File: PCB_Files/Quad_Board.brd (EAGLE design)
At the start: 129.2 x 80 mm, 32 parts, among them IC2 LM317MB, Q1 32.768kHz, Q2 KX-7 48MHz

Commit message: Board Layout Under Progress
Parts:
- removed 12V_PDB, JP1: (no value), pinhead:1X02
- removed U$2: NAZE32_FC, Naze32_FCBoard:NAZE32_BOARD_FOOTPRINT
- added LEVEL_TRANSLATOR1, LEVEL_TRANSLATOR_@, LEVEL_TRANSLATOR_@1: (no value), SparkFun-DigitalIC:SO14
- added MOTHERBOPARD_TX: (no value), pinhead:1X02
- added NAZE32_PINHEAD: (no value), pinhead:1X10
- added R4, R5, R6: (no value), eagle-ltspice:R2512
- added SJ1, SJ2, SJ3: SOLDERJUMPERNC2, SparkFun-Passives:SJ_2S-NOTRACE
- moved Q2 209.3 mm to (55.9, 44.5), turned to 90 degrees
- moved C5 209.1 mm to (54.6, 29.2), turned to 90 degrees
- moved C6 208.3 mm to (54.6, 34.3), turned to 90 degrees
- moved R3 207.8 mm to (54.6, 39.4), turned to 90 degrees
- moved MINIJTAG 206.0 mm to (64.8, 14.0), turned to 270 degrees
- moved C8 201.9 mm to (49.5, 29.2), turned to 90 degrees
- moved C11 201.1 mm to (49.5, 34.3), turned to 90 degrees
- moved C12 200.6 mm to (49.5, 39.4), turned to 90 degrees
- moved C13 200.3 mm to (49.5, 44.5), turned to 90 degrees
- moved L1 192.8 mm to (43.2, 30.5), turned to 90 degrees
- moved C3 192.2 mm to (43.2, 34.3), turned to 90 degrees
- moved C4 191.6 mm to (43.2, 39.4), turned to 90 degrees
- moved C7 191.3 mm to (43.2, 44.5), turned to 90 degrees
- moved Q1 183.0 mm to (48.3, 16.5), turned to 270 degrees
- moved R1 182.9 mm to (57.1, 6.35), turned to 90 degrees
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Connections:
- net N$17 renamed P10.5_V
- removed net 12VDC: 12V_PDB.1
- removed net N$13: ULTRA3.2
- removed net N$3: ULTRA1.2
- removed net N$4: 12V_PDB.2
- removed net N$5: ULTRA3.3
- removed net N$6: MSP1.75
- removed net P5.4_IO_J3.29: MSP1.68, ULTRA5.2
- removed net P5.5_IO_J3.30: MSP1.69, ULTRA6.2
- removed net P5.6_PWM_J4.37: MSP1.70, ULTRA5.3
- removed net P5.7_IO_J2.17: MSP1.71, ULTRA6.3
- removed net P6.6_CAPTURE_J4.36: MSP1.80
- removed net P6.7_CAPTURE_J4.35: MSP1.81
- removed net P9.1: MSP1.53, ULTRA2.2
- new net 3.3V: LEVEL_TRANSLATOR1.1, LEVEL_TRANSLATOR_@.1, LEVEL_TRANSLATOR_@1.1, SJ1.2, SJ2.2, SJ3.2
- new net 5V: LEVEL_TRANSLATOR1.14, LEVEL_TRANSLATOR_@.14, LEVEL_TRANSLATOR_@1.14
- new net N$1: MSP1.53
- new net N$19: MSP1.68
- new net N$20: MSP1.69
- new net N$25: MSP1.24
- new net N$26: MSP1.25
- new net OE: LEVEL_TRANSLATOR1.8, LEVEL_TRANSLATOR_@.8, LEVEL_TRANSLATOR_@1.8, R4.2, R5.2, R6.2, SJ1.1, SJ2.1, SJ3.1
- new net P10.3_GPIO5V: LEVEL_TRANSLATOR_@.10, ULTRA4.3
- new net P10.4_5V: LEVEL_TRANSLATOR_@.12, ULTRA3.3
- new net P10.5_5V: LEVEL_TRANSLATOR_@.11
- new net P5.6: LEVEL_TRANSLATOR_@1.2, MSP1.70
- new net P5.6_5V: LEVEL_TRANSLATOR_@1.13, ULTRA5.3
- new net P5.7: LEVEL_TRANSLATOR_@1.3
- new net P5.7/TA2.2/VREF-/VEREF-/C1.6: MSP1.71
- new net P5.7_5V: LEVEL_TRANSLATOR_@1.12, ULTRA5.2
- new net P6.6: LEVEL_TRANSLATOR_@1.4, MSP1.80
- new net P6.6_5V: LEVEL_TRANSLATOR_@1.11, ULTRA6.3
- new net P6.7: LEVEL_TRANSLATOR_@1.5, MSP1.81
- new net P6.7_5V: LEVEL_TRANSLATOR_@1.10, ULTRA6.2
- new net P8.0_5V: LEVEL_TRANSLATOR1.13, ULTRA1.2
- new net P8.1_5V: LEVEL_TRANSLATOR1.12, ULTRA1.3
- new net P8.2_5V: LEVEL_TRANSLATOR1.11
- new net P8.3_5V: ULTRA2.2
- new net P9.2_5V: LEVEL_TRANSLATOR1.10, ULTRA2.3
- new net P9.3: LEVEL_TRANSLATOR_@.2, MSP1.75
- new net P9.3_5V: LEVEL_TRANSLATOR_@.13, ULTRA3.2
- net 5VDC: now also NAZE32_PINHEAD.2; no longer U$2.5V
- net GND: now also LEVEL_TRANSLATOR1.7, LEVEL_TRANSLATOR_@.7, LEVEL_TRANSLATOR_@1.7, NAZE32_PINHEAD.1, R4.1, R5.1, R6.1; no longer U$2.GND
- net N$10: now also MOTHERBOPARD_TX.2; no longer JP1.2
- net P10.3: now also LEVEL_TRANSLATOR_@.5
- net P10.4: now also LEVEL_TRANSLATOR_@.3; no longer MSP1.24
- net P10.5: now also LEVEL_TRANSLATOR_@.4; no longer MSP1.25, ULTRA4.3
- net P2.4_PWM_J4.38: now also NAZE32_PINHEAD.10; no longer U$2.8
- net P2.5_PWM_J2.19: now also NAZE32_PINHEAD.9; no longer U$2.7
- net P2.6_PWM_J4.39: now also NAZE32_PINHEAD.8; no longer U$2.6
- net P2.7_PWM_J4.40: no longer U$2.LED/5
- net P3.3_UTXD_J1.4: now also MOTHERBOPARD_TX.1
- net P7.4: now also NAZE32_PINHEAD.6; no longer U$2.U2RX/4
- net P7.5: now also NAZE32_PINHEAD.5; no longer U$2.U2TX/3
- net P7.6: now also NAZE32_PINHEAD.4; no longer U$2.2
- net P7.7: now also NAZE32_PINHEAD.3; no longer U$2.PPM
- net P8.0: now also LEVEL_TRANSLATOR1.2
- net P8.1: now also LEVEL_TRANSLATOR1.3, LEVEL_TRANSLATOR1.4
- net P8.2: no longer ULTRA1.3
- net P9.2: now also LEVEL_TRANSLATOR1.5; no longer ULTRA2.3
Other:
- board size 129.2 x 80 mm -> 114 x 80 mm

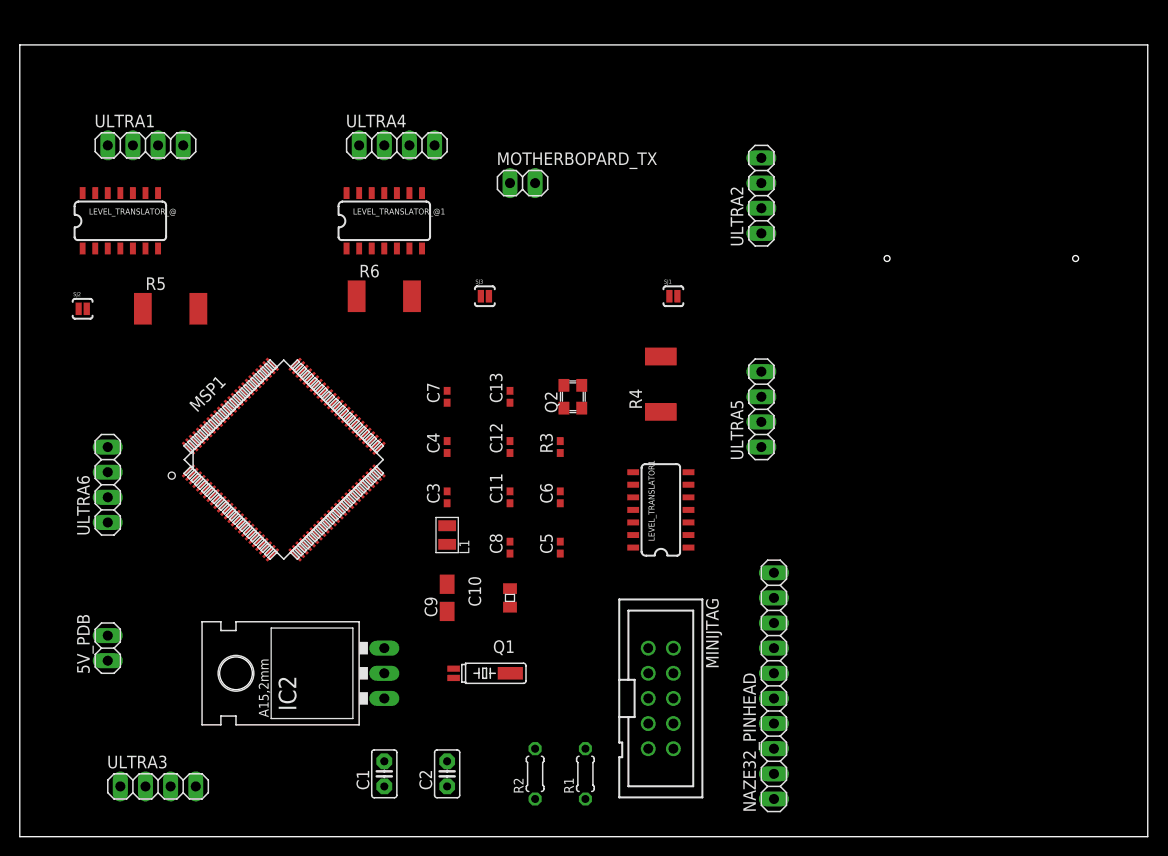
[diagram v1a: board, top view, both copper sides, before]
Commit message: Board Layout in Routing Stage
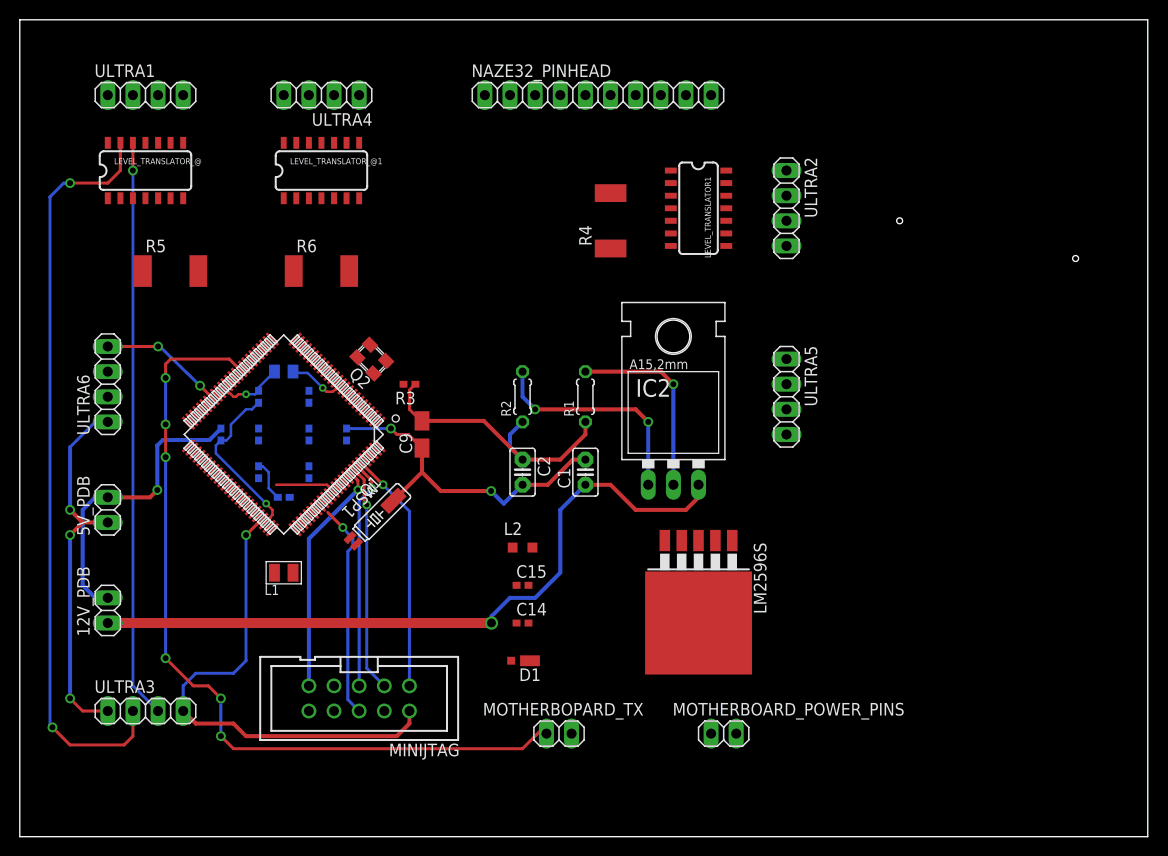
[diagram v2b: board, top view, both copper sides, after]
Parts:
- removed SJ1, SJ2, SJ3: SOLDERJUMPERNC2, SparkFun-Passives:SJ_2S-NOTRACE
- added 12V_PDB, MOTHERBOARD_POWER_PINS: (no value), pinhead:1X02
- added C14: 680u, rcl:0402
- added C15: 220u, rcl:0402
- added D1: PD3S160, diode:POWERDI323
- added L2: 33u, resistor:L2012C
- added LM2596S: LM2596S, national-semiconductor:TO263-5
- moved NAZE32_PINHEAD 62.3 mm to (58.4, 74.9), turned to 0 degrees
- moved MOTHERBOPARD_TX 55.7 mm to (54.5, 10.4)
- moved IC2 40.2 mm to (66.0, 39.4), turned to 0 degrees
- moved R2 38.1 mm to (50.8, 44.5)
- moved R1 38.1 mm to (57.1, 44.5)
- moved C1 36.6 mm to (57.1, 36.8)
- moved C10 32.3 mm to (26.7, 47.0), flipped to the bottom, turned to 0 degrees
- moved C2 31.4 mm to (50.8, 36.8), turned to 270 degrees
- moved C8 31.4 mm to (20.3, 40.6), flipped to the bottom
- moved LEVEL_TRANSLATOR1 30.7 mm to (68.6, 63.5), turned to 270 degrees
- moved MINIJTAG 30.5 mm to (34.3, 14.0), turned to 180 degrees
- moved C5 28.4 mm to (26.7, 34.3), flipped to the bottom, turned to 0 degrees
- moved C6 22.5 mm to (33.0, 40.6), flipped to the bottom
- moved Q2 20.7 mm to (35.6, 48.3), turned to 135 degrees
- moved C11 20.5 mm to (29.2, 36.8), flipped to the bottom
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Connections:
- net P3.2/PM_UCA2RXD/PM_UCA2SOMI renamed N$10
- removed net N$25: MSP1.24
- removed net N$26: MSP1.25
- removed net OE: LEVEL_TRANSLATOR1.8, LEVEL_TRANSLATOR_@.8, LEVEL_TRANSLATOR_@1.8, R4.2, R5.2, R6.2, SJ1.1, SJ2.1, SJ3.1
- removed net P5.7/TA2.2/VREF-/VEREF-/C1.6: MSP1.71
- removed net P8.3_5V: ULTRA2.2
- new net 12VDC: 12V_PDB.1, C1.1, C14.1, IC2.3, LM2596S.1
- new net MOTHEROARD_V+: C15.1, L2.2, LM2596S.4, MOTHERBOARD_POWER_PINS.1
- new net N$4: D1.C, L2.1, LM2596S.2
- net 3.3V: now also LEVEL_TRANSLATOR1.8, LEVEL_TRANSLATOR_@.8, LEVEL_TRANSLATOR_@1.8, R4.2, R5.2, R6.2; no longer SJ1.2, SJ2.2, SJ3.2
- net 5VDC: now also 5V_PDB.1; no longer C1.1, IC2.3
- net GND: now also 12V_PDB.2, C14.2, C15.2, D1.A, LM2596S.3, LM2596S.5, MOTHERBOARD_POWER_PINS.2
- net P10.4: now also MSP1.24
- net P10.5: now also MSP1.25
- net P2.7_PWM_J4.40: now also NAZE32_PINHEAD.7
- net P5.7: now also MSP1.71
- net P8.2_5V: now also ULTRA2.2
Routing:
- net GND: track 0.00 -> 144.5 mm, vias 0 -> 7
- net P3.3_UTXD_J1.4: track 0.00 -> 84.4 mm, vias 0 -> 6
- net P9.3_5V: track 0.00 -> 76.5 mm, vias 0 -> 2
- net 12VDC: track 0.00 -> 72.4 mm, vias 0 -> 1
- net P10.4_5V: track 0.00 -> 58.5 mm, vias 0 -> 1
- net 3V3: track 0.00 -> 42.2 mm, vias 0 -> 1
- net 5VDC: track 0.00 -> 38.2 mm, vias 0 -> 3
- net TCK_SWCLK: track 0.00 -> 24.5 mm, vias 0 -> 1
- net TDI: track 0.00 -> 23.8 mm, vias 0 -> 1
- net TMS_SWDIO: track 0.00 -> 23.2 mm, vias 0 -> 1
- net TDO_SWO: track 0.00 -> 23.0 mm, vias 0 -> 1
- net N$28: track 0.00 -> 22.6 mm, vias 0 -> 2
- net !RST: track 0.00 -> 21.8 mm, vias 0 -> 1
- net N$29: track 0.00 -> 19.6 mm, vias 0 -> 1
- net N$2: track 0.00 -> 6.07 mm
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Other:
- board size 114 x 80 mm -> 114 x 82.5 mm

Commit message: PCB Layout Rev1 90% done
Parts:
- added R7: (no value), rcl:0204/5
- added U$1: TXS0102, TXS0102-bi-directional-translator:SM8
- moved C15 7.41 mm to (57.1, 29.2), turned to 270 degrees
- moved C14 6.35 mm to (57.1, 21.6), turned to 90 degrees
- moved D1 3.81 mm to (50.8, 21.6), turned to 270 degrees
- moved R4 1.80 mm to (61.0, 63.5)
- moved ULTRA5 1.27 mm to (77.5, 45.7)
- turned C1 to 270 degrees
- turned L2 to 90 degrees
- turned R5 to 180 degrees
- turned R6 to 180 degrees
- renumbered LEVEL_TRANSLATOR_@ to LEVEL_TRANSLATOR_2, LEVEL_TRANSLATOR_@1 to LEVEL_TRANSLATOR_3
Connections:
- removed net N$10: MSP1.34
- removed net N$3: MOTHERBOPARD_TX.2
- removed net P3.3_UTXD_J1.4: MOTHERBOPARD_TX.1, MSP1.35
- new net A1: MSP1.35, U$1.5
- new net A2: MOTHERBOPARD_TX.1, U$1.4
- new net B1: MSP1.34, U$1.8
- new net B2: MOTHERBOPARD_TX.2, U$1.1
- new net OE: R7.1, U$1.6
- net 3V3: now also U$1.7
- net 5V: now also U$1.3
- net GND: now also R7.2, U$1.2
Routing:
- net GND: track 144.5 -> 345.1 mm, vias 7 -> 22
- net 5V: track 0.00 -> 85.2 mm, vias 0 -> 6
- net P9.2: track 0.00 -> 84.7 mm, vias 0 -> 6
- net P3.3_UTXD_J1.4: track 84.4 -> 0.00 mm, vias 6 -> 0
- net 3.3V: track 0.00 -> 83.8 mm, vias 0 -> 12
- net P8.1: track 0.00 -> 77.5 mm, vias 0 -> 4
- net P8.0_5V: track 0.00 -> 70.3 mm, vias 0 -> 4
- net P2.4_PWM_J4.38: track 0.00 -> 70.3 mm, vias 0 -> 3
- net 5VDC: track 38.2 -> 106.2 mm, vias 3 -> 4
- net P9.3: track 0.00 -> 66.5 mm, vias 0 -> 4
- net P2.5_PWM_J2.19: track 0.00 -> 65.8 mm, vias 0 -> 1
- net P2.6_PWM_J4.39: track 0.00 -> 65.0 mm, vias 0 -> 5
- net P7.4: track 0.00 -> 58.9 mm, vias 0 -> 1
- net P7.5: track 0.00 -> 57.4 mm, vias 0 -> 1
- net P2.7_PWM_J4.40: track 0.00 -> 56.9 mm, vias 0 -> 1
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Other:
- board size 114 x 82.5 mm -> 83.5 x 78.7 mm
- board text added: "3-DMQ System PCB Layout"
- board text added: "rev 1.0"

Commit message: MCU Icaps routing remaining
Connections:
- net N$19 renamed P5.4/A1
- net N$20 renamed P5.5/A0
- net P1.0_LED1 renamed P1.0/UCA0STE
- net P1.1_BUTTON1 renamed P1.1/UCA0CLK
- net P1.2_BCLUART_RXD renamed P1.2/UCA0RXD/UCA0SOMI
- net P1.3_BCLUART_TXD renamed P1.3/UCA0TXD/UCA0SIMO
- net P1.4_BUTTON2 renamed P1.4/UCB0STE
- net P1.5_SPICLK_J1.7 renamed P1.5/UCB0CLK
- net P1.6_SPIMOSI_J2.15 renamed P1.6/UCB0SIMO/UCB0SDA
- net P1.7_SPIMISO_J2.14 renamed P1.7/UCB0SOMI/UCB0SCL
- net P2.0_RGBLED_RED renamed P2.0/PM_UCA1STE
- net P2.1_RGBLED_GREEN renamed P2.1/PM_UCA1CLK
- net P2.2_RGBLED_BLUE renamed P2.2/PM_UCA1RXD/PM_UCA1SOMI
- net P2.3_IO_J4.34 renamed P2.3/PM_UCA1TXD/PM_UCA1SIMO
- net P3.0_IO_J2.18 renamed P3.0/PM_UCA2STE
- net P3.1_BCLUART_RTS renamed P3.1/PM_UCA2CLK
- net P3.4_BCLUART_CTS renamed P3.4/PM_UCB2STE
- net P3.5_IO_J4.32 renamed P3.5/PM_UCB2CLK
- net P3.6_IO_J2.11 renamed P3.6/PM_UCB2SIMO/PM_UCB2SDA
- net P3.7_IO_J4.31 renamed P3.7/PM_UCB2SOMI/PM_UCB2SCL
- net P4.0_A13_J3.24 renamed P4.0/A13
- net P4.1_IO_J1.5 renamed P4.1/A12
- net P4.2_A11_J3.25 renamed P4.2/ACLK/TA2CLK/A11
- net P4.3_A10_J1.6 renamed P4.3/MCLK/RTCCLK/A10
- net P4.4_A9_J3.26 renamed P4.4/HSMCLK/SVMHOUT/A9
- net P4.5_A8_J3.27 renamed P4.5/A8
- net P4.6_IO_J1.8 renamed P4.6/A7
- net P4.7_A6_J3.28 renamed P4.7/A6
- net P5.0_IO_J2.13 renamed P5.0/A5
- net P5.1_IO_J4.33 renamed P5.1/A4
- net P5.2_IO_J2.12 renamed P5.2/A3
- net P5.3 renamed P5.3/A2
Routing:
- net P8.1_5V: track 0.00 -> 81.4 mm, vias 0 -> 3
- net 5V: track 85.2 -> 155.5 mm, vias 6 -> 10
- net 5VDC: track 106.2 -> 162.1 mm, vias 4 -> 5
- net 3.3V: track 83.8 -> 112.3 mm
- net GND: track 345.1 -> 355.7 mm

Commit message: PCB Updates
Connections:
- net N$1 renamed P9.1/A16
- net P10.0 renamed P10.0/UCB3STE
- net P10.1 renamed P10.1/UCB3CLK
- net P10.2 renamed P10.2/UCB3SIMO/UCB3SDA
- net P6.0_A15_J1.2 renamed P6.0/A15
- net P6.1_A14_J3.23 renamed P6.1/A14
- net P6.2 renamed P6.2/UCB1STE/C1.5
- net P6.3 renamed P6.3/UCB1CLK/C1.4
- net P6.4_I2CSDA_J1.10 renamed P6.4/UCB1SIMO/UCB1SDA/C1.3
- net P6.5_I2CSCL_J1.9 renamed P6.5/UCB1SOMI/UCB1SCL/C1.2
- net P7.0 renamed P7.0/PM_SMCLK/PM_DMAE0
- net P7.1 renamed P7.1/PM_C0OUT/PM_TA0CLK
- net P7.2 renamed P7.2/PM_C1OUT/PM_TA1CLK
- net P8.3 renamed P8.3/TA3CLK/A22
- net P8.4 renamed P8.4/A21
- net P8.5 renamed P8.5/A20
- net P8.6 renamed P8.6/A19
- net P8.7 renamed P8.7/A18
- net P9.0 renamed P9.0/A17
- net P9.4 renamed P9.4/UCA3STE
- net P9.5 renamed P9.5/UCA3CLK
- net P9.6 renamed P9.6/UCA3RXD/UCA3SOMI
- net P9.7 renamed P9.7/UCA3TXD/UCA3SIMO
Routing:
- net P5.6_5V: track 0.00 -> 71.1 mm, vias 0 -> 6
- net 5VDC: track 162.1 -> 182.0 mm
- net GND: track 355.7 -> 369.8 mm, vias 22 -> 24

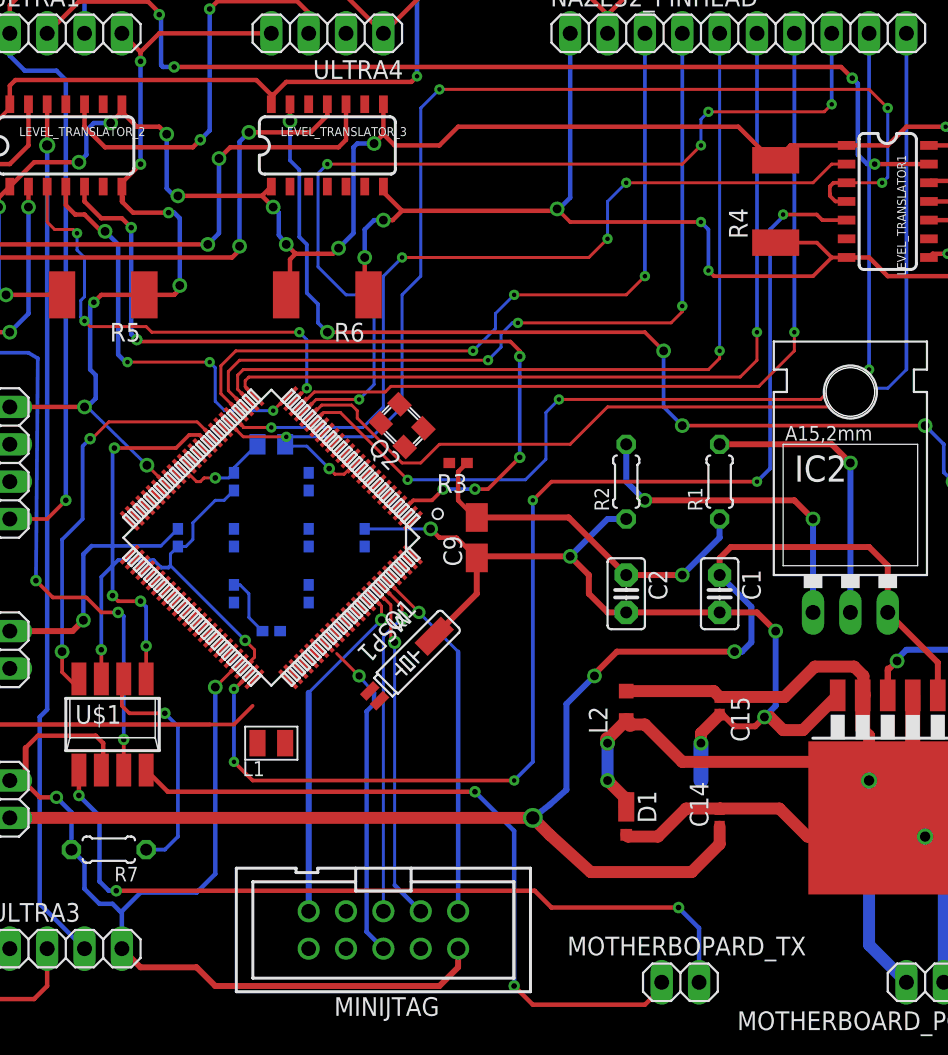
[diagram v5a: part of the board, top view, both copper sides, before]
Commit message: Added Battery Monitroing Circuit
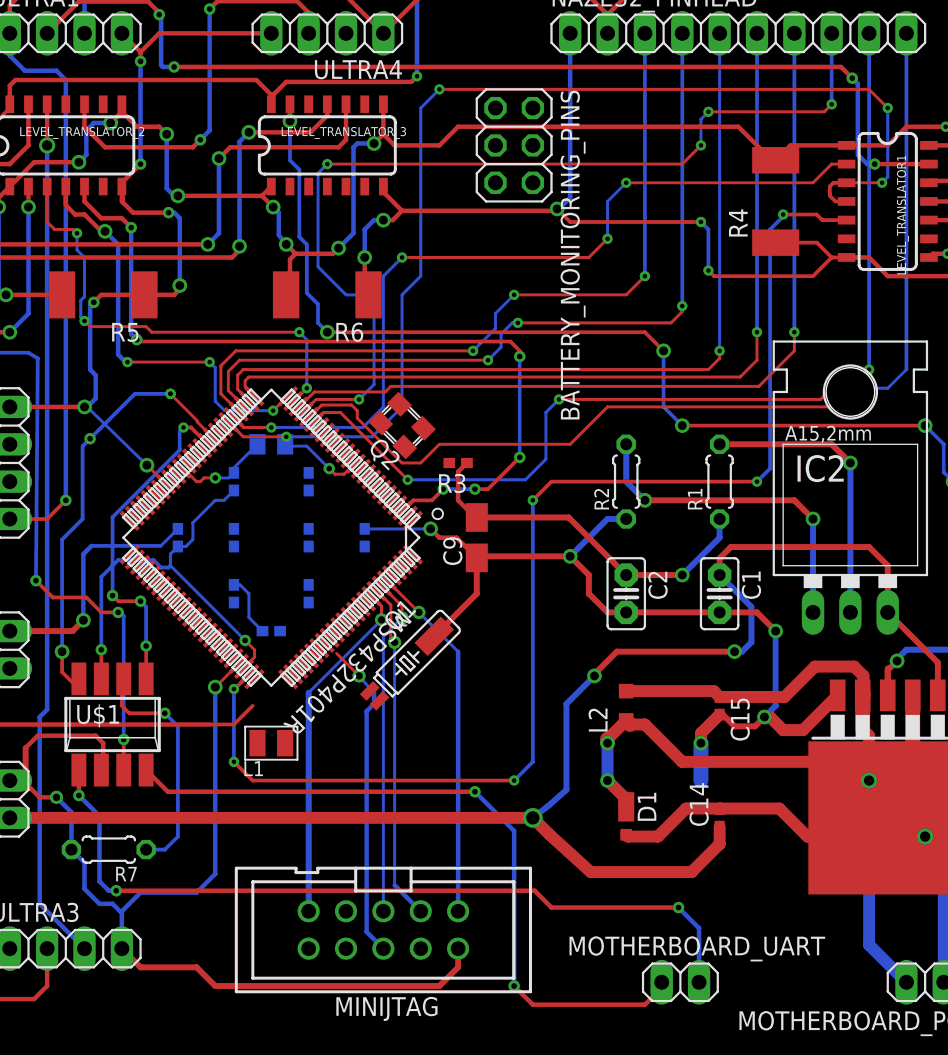
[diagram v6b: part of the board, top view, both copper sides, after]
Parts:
- added BATTERY_MONITORING_PINS: (no value), pinhead:2X03
- renumbered MOTHERBOPARD_TX to MOTHERBOARD_UART, MSP1 to MSP432P401R
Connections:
- removed net P3.6/PM_UCB2SIMO/PM_UCB2SDA: MSP432P401R.38
- removed net P3.7/PM_UCB2SOMI/PM_UCB2SCL: MSP432P401R.39
- new net P2.2_RX: BATTERY_MONITORING_PINS.1
- new net P3.6_SDA: BATTERY_MONITORING_PINS.3, MSP432P401R.38
- new net P3.7_SCL: BATTERY_MONITORING_PINS.4, MSP432P401R.39
- net 3V3: now also BATTERY_MONITORING_PINS.5
- net GND: now also BATTERY_MONITORING_PINS.2, BATTERY_MONITORING_PINS.6
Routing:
- net B1: track 27.3 -> 29.0 mm, vias 2 -> 4
- net A1: track 24.5 -> 23.0 mm
